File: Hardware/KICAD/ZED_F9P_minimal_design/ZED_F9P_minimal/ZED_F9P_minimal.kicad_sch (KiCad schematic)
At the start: 28 parts, among them J1 Conn_Coaxial_Small, J2 DF11-18DS-2DSA06, U1 OPA2365AID, U2 LM1086IT-ADJ/NOPB, U3 ZED-F9P

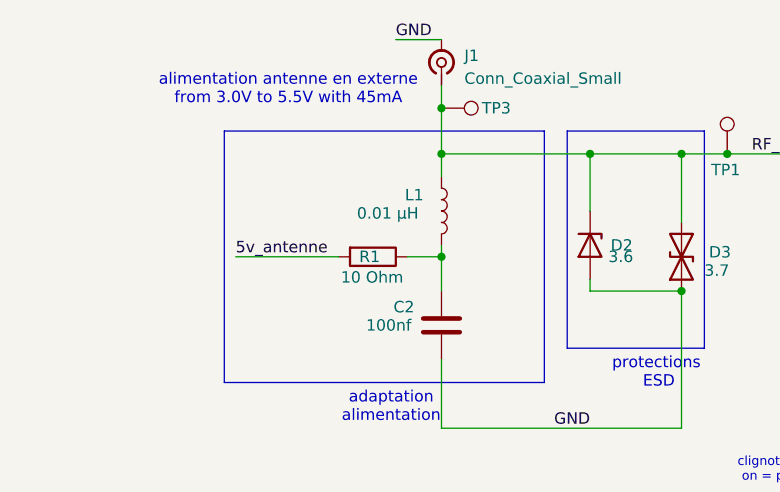
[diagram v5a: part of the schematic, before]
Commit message: rooting PCB
added ground plane, rooted and shaped critical input signal for 50ohm impedance
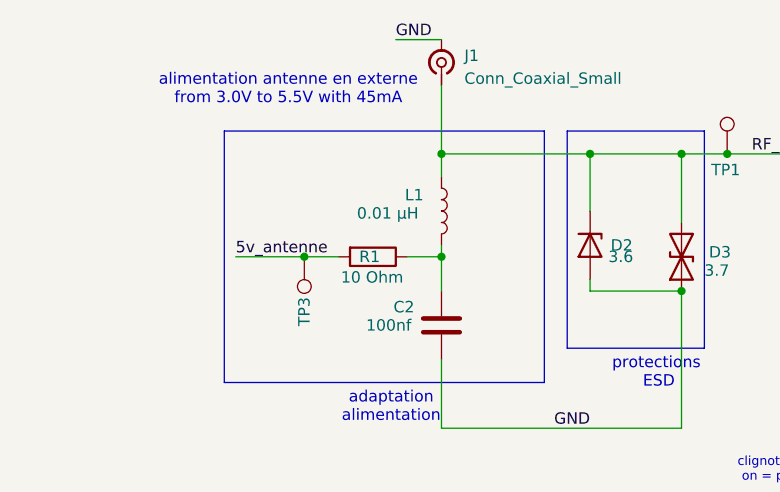
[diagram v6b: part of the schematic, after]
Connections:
- net 5v_antenne: now also TP3.1
- net RF_IN: no longer TP3.1
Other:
- moved on the sheet: TP3
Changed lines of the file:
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@@
 	)
 	(junction
-		(at 78.74 35.56)
-		(diameter 0)
-		(color 0 0 0 0)
-	)
-	(junction
 		(at 105.41 40.64)
 		(diameter 0)
@@
 	)
 	(junction
+		(at 63.5 52.07)
+		(diameter 0)
+		(color 0 0 0 0)
+	)
+	(junction
 		(at 78.74 40.64)
 		(diameter 0)
@@
 	(wire
 		(pts
-			(xy 78.74 35.56) (xy 78.74 40.64)
+			(xy 78.74 33.02) (xy 78.74 40.64)
 		)
 		(stroke
@@
 	(wire
 		(pts
-			(xy 78.74 33.02) (xy 78.74 35.56)
-		)
-		(stroke
-			(width 0)
-			(type default)
-		)
-	)
-	(wire
-		(pts
 			(xy 44.45 134.62) (xy 53.34 134.62)
 		)
@@
 	(wire
 		(pts
+			(xy 63.5 52.07) (xy 67.31 52.07)
+		)
+		(stroke
+			(width 0)
+			(type default)
+		)
+	)
+	(wire
+		(pts
 			(xy 115.57 100.33) (xy 115.57 104.14)
 		)
@@
 	(wire
 		(pts
-			(xy 55.88 52.07) (xy 67.31 52.07)
+			(xy 55.88 52.07) (xy 63.5 52.07)
 		)
 		(stroke
@@
 	(symbol
 		(lib_id "Connector:TestPoint")
-		(at 78.74 35.56 270)
+		(at 63.5 52.07 180)
 		(unit 1)
 		(exclude_from_sim no)
@@
 		(dnp no)
 		(property "Reference" "TP3"
-			(at 84.836 35.56 90)
+			(at 63.5 58.166 90)
 			(effects
 				(font
@@
 		)
 		(property "Value" "TestPoint"
-			(at 82.55 37.338 90)
+			(at 61.722 55.88 90)
 			(effects
 				(font
@@
 		)
 		(property "Footprint" "TestPoint:CONN1_5011_KEY"
-			(at 78.74 40.64 0)
+			(at 58.42 52.07 0)
 			(effects
 				(font
@@
 		)
 		(property "Datasheet" "~"
-			(at 78.74 40.64 0)
+			(at 58.42 52.07 0)
 			(effects
 				(font
@@
 		)
 		(property "Description" "test point"
-			(at 78.74 35.56 0)
+			(at 63.5 52.07 0)
 			(effects
 				(font
@@
 		)
 		(property "Height" ""
-			(at 78.74 35.56 0)
+			(at 63.5 52.07 0)
 			(effects
 				(font
@@
 		)
 		(property "Manufacturer_Name" ""
-			(at 78.74 35.56 0)
+			(at 63.5 52.07 0)
 			(effects
 				(font
@@
 		)
 		(property "Manufacturer_Part_Number" ""
-			(at 78.74 35.56 0)
+			(at 63.5 52.07 0)
 			(effects
 				(font
@@
 		)
 		(property "Mouser Part Number" ""
-			(at 78.74 35.56 0)
+			(at 63.5 52.07 0)
 			(effects
 				(font
@@
 		)
 		(property "Mouser Price/Stock" ""
-			(at 78.74 35.56 0)
+			(at 63.5 52.07 0)
 			(effects
 				(font

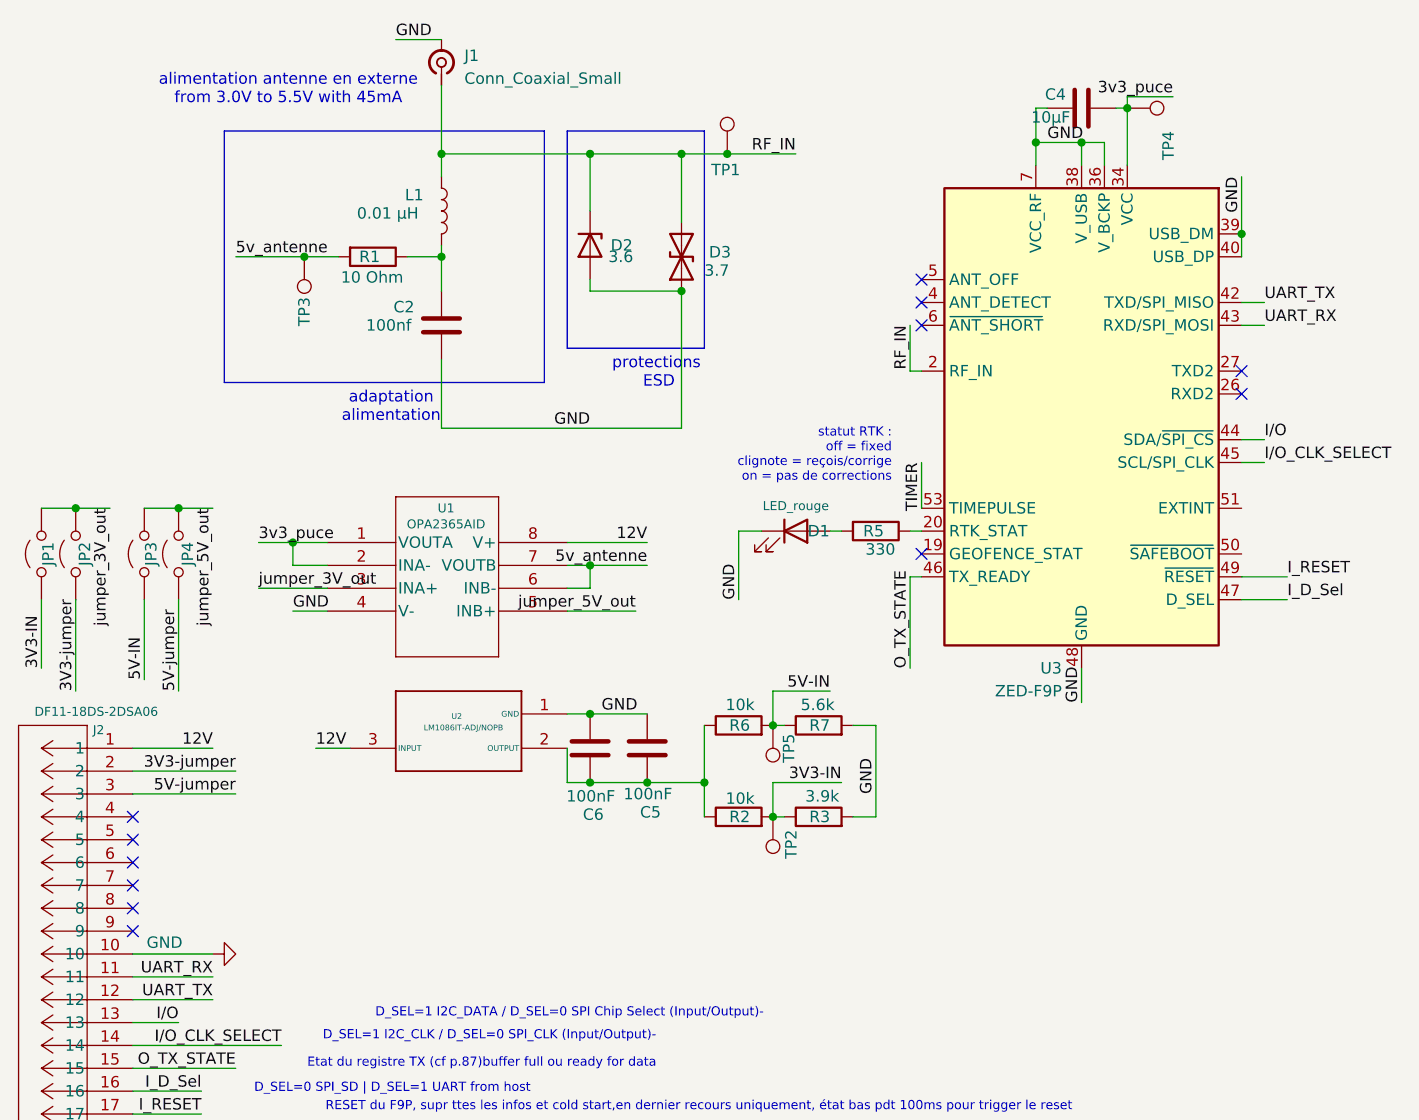
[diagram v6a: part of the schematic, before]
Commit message: corrections
added SMA connector and  actualised pin connector footprint
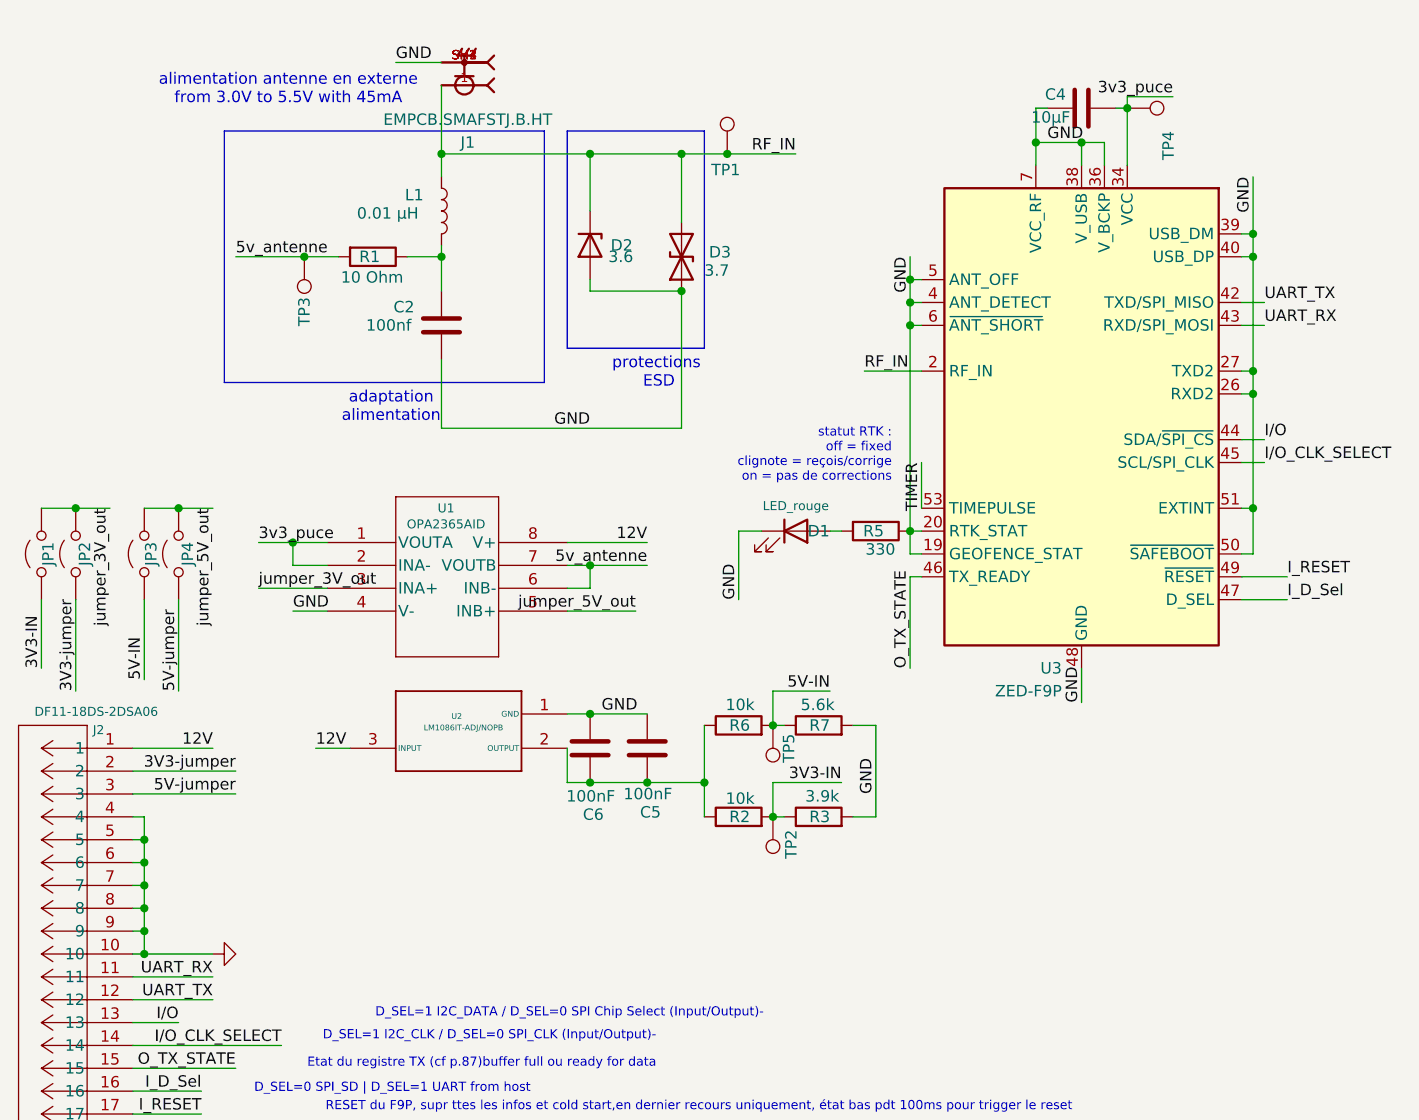
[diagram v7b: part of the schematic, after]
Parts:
- removed J1: Conn_Coaxial_Small, SMA:RFSOLUTIONS_CON-SMA-EDGE-S, symbol Connector:Conn_Coaxial_Small
- added J1: EMPCB.SMAFSTJ.B.HT, Connector:TAOGLAS_EMPCB.SMAFSTJ.B.HT, symbol SMA:EMPCB.SMAFSTJ.B.HT
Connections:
- net GND: now also J2.4, J2.5, J2.6, J2.7, J2.8, J2.9, R5.1, U3.19 (GEOFENCE_STAT), U3.20 (RTK_STAT), U3.26 (RXD2), U3.27 (TXD2), U3.4 (ANT_DETECT), U3.5 (ANT_OFF), U3.50 (~{SAFEBOOT}), U3.51 (EXTINT), U3.6 (~{ANT_SHORT}), J1.SH1, J1.SH2, J1.SH3, J1.SH4
- net RF_IN: now also J1.1
- no-connect marks 12 -> 0

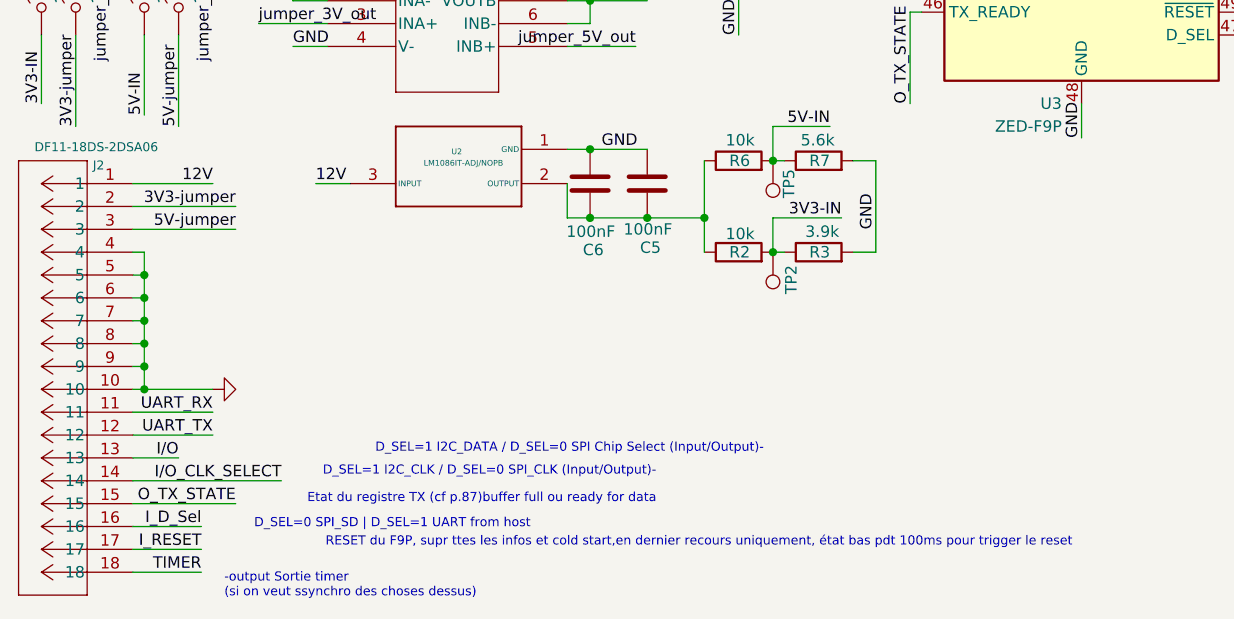
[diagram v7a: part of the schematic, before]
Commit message: PCB rooting
finalised PCB rooting
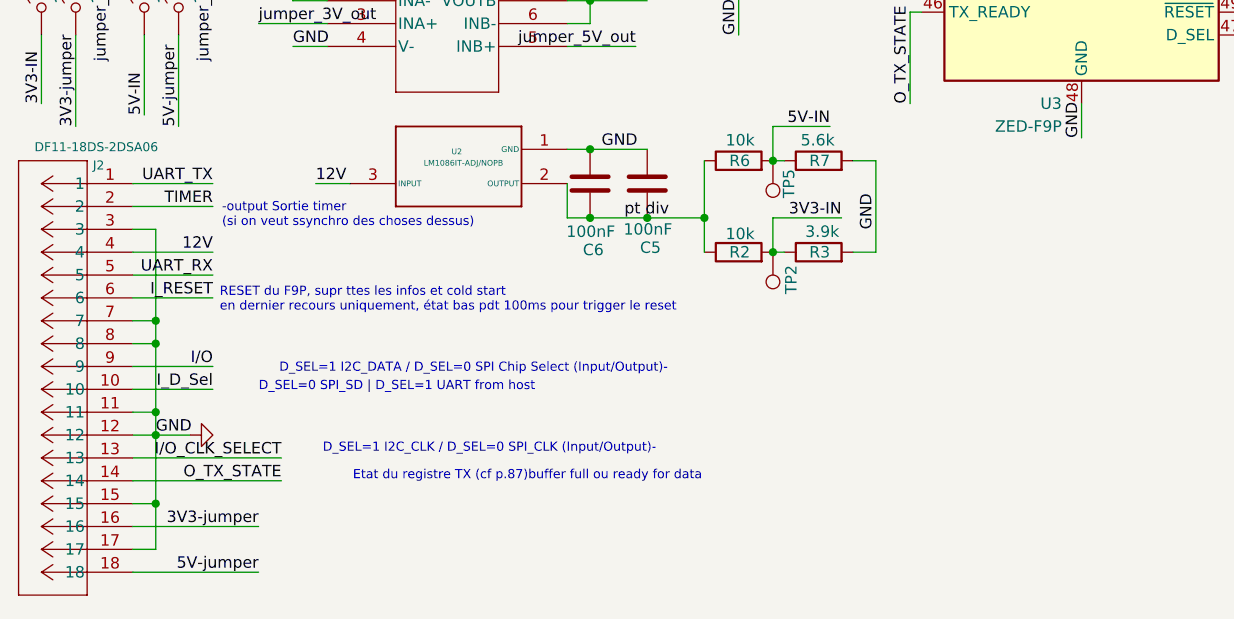
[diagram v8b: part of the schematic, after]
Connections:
- net 12V: now also J2.4; no longer J2.1
- net 3V3-jumper: now also J2.16; no longer J2.2
- net 5V-jumper: now also J2.18; no longer J2.3
- net GND: now also J2.11, J2.12, J2.15, J2.17, J2.3; no longer J2.10, J2.4, J2.5, J2.6, J2.9
- net I_D_Sel: now also J2.10; no longer J2.16
- net I_RESET: now also J2.6; no longer J2.17
- net I/O : now also J2.9; no longer J2.13
- net I/O_CLK_SELECT: now also J2.13; no longer J2.14
- net O_TX_STATE: now also J2.14; no longer J2.15
- net TIMER: now also J2.2; no longer J2.18
- net UART_RX: now also J2.5; no longer J2.11
- net UART_TX: now also J2.1; no longer J2.12
- net pt div: now reaches C5.1, C6.1, R2.1, R6.1, U2.2 (OUTPUT)
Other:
- note added: "RESET du F9P, supr ttes les infos et cold start en dernier recours uniquement, état bas pdt 100ms pour trigger le reset"
- note removed: "RESET du F9P, supr ttes les infos et cold start,en dernier recours uniquement, état bas pdt 100ms pour trigger le reset"
